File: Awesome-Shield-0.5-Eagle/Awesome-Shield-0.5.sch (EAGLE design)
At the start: 24 parts, among them J1 ARDUINO_R3_SHIELDUNO_R3_SHIEL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, SW1 SPST_TACT-EVQQ2

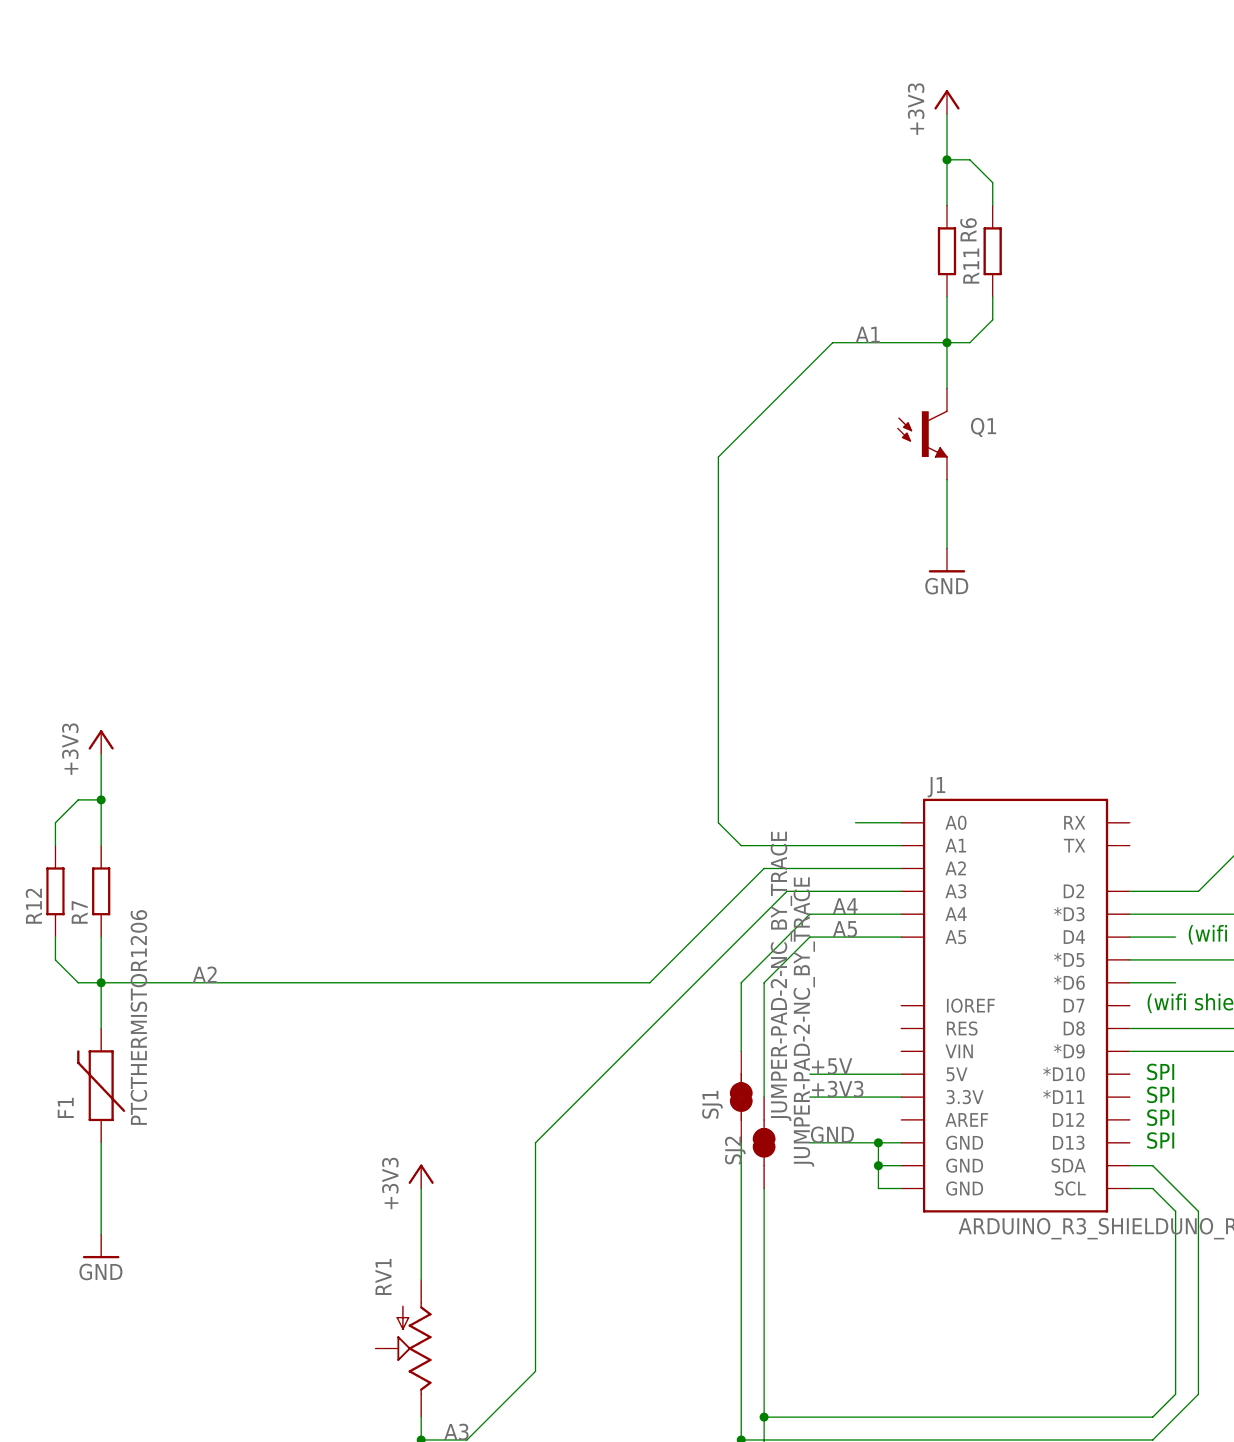
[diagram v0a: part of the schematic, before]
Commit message: changed thermistor, photodiode, and potentiometer to be powered off IOREF
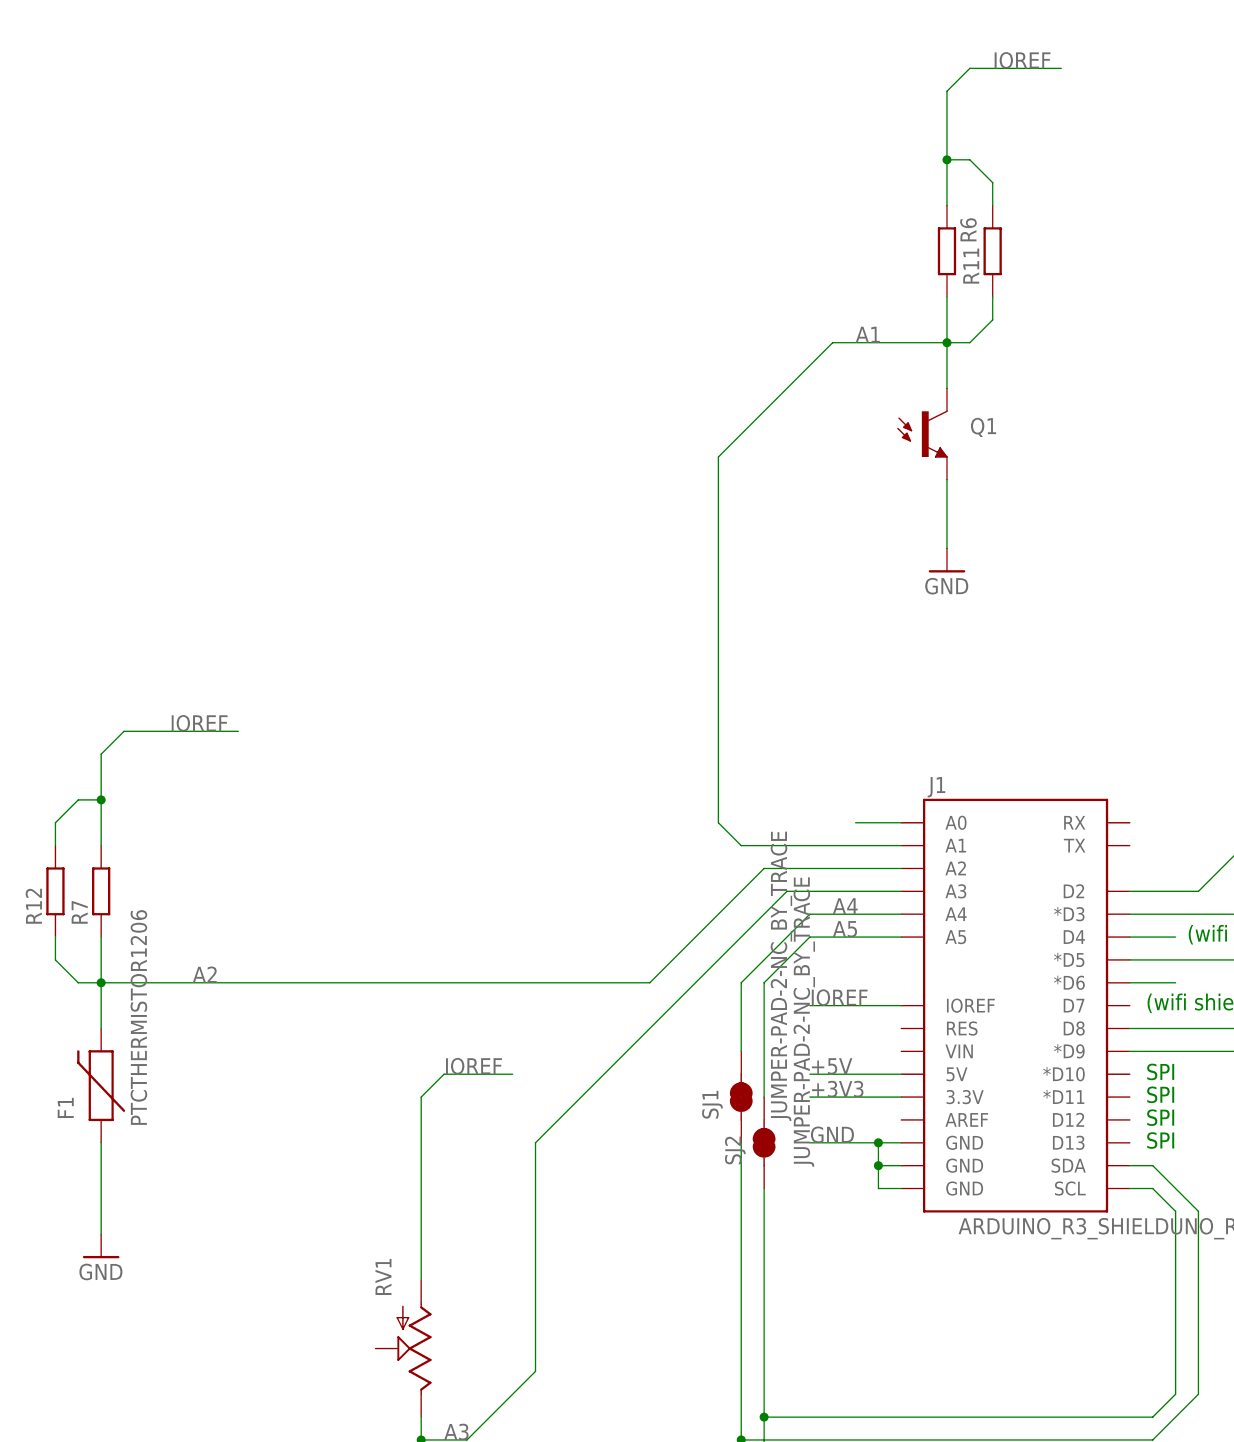
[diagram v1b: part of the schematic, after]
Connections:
- new net IOREF: J1.IOREF, R11.2, R12.2, R6.1, R7.2, RV1.A
- net +3V3: no longer R11.2, R12.2, R6.1, R7.2, RV1.A
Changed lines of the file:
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@@
 <part name="GND3" library="supply1" deviceset="GND" device=""/>
 <part name="GND4" library="supply1" deviceset="GND" device=""/>
-<part name="+3V1" library="supply1" deviceset="+3V3" device=""/>
-<part name="+3V2" library="supply1" deviceset="+3V3" device=""/>
-<part name="+3V3" library="supply1" deviceset="+3V3" device=""/>
 <part name="GND5" library="supply1" deviceset="GND" device=""/>
 <part name="GND6" library="supply1" deviceset="GND" device=""/>
@@
 <instance part="GND3" gate="1" x="93.98" y="101.6"/>
 <instance part="GND4" gate="1" x="129.54" y="68.58"/>
-<instance part="+3V1" gate="G$1" x="93.98" y="160.02"/>
-<instance part="+3V2" gate="G$1" x="129.54" y="111.76"/>
-<instance part="+3V3" gate="G$1" x="187.96" y="231.14"/>
 <instance part="GND5" gate="1" x="269.24" y="190.5"/>
 <instance part="GND6" gate="1" x="165.1" y="45.72"/>
@@
 <net name="+3V3" class="0">
 <segment>
-<pinref part="+3V3" gate="G$1" pin="+3V3"/>
-<pinref part="R6" gate="G$1" pin="1"/>
-<wire x1="187.96" y1="228.6" x2="187.96" y2="223.52" width="0.1524" layer="91"/>
-<pinref part="R11" gate="G$1" pin="2"/>
-<wire x1="187.96" y1="223.52" x2="187.96" y2="218.44" width="0.1524" layer="91"/>
-<wire x1="193.04" y1="218.44" x2="193.04" y2="220.98" width="0.1524" layer="91"/>
-<wire x1="193.04" y1="220.98" x2="190.5" y2="223.52" width="0.1524" layer="91"/>
-<wire x1="190.5" y1="223.52" x2="187.96" y2="223.52" width="0.1524" layer="91"/>
-<junction x="187.96" y="223.52"/>
-</segment>
-<segment>
-<pinref part="+3V1" gate="G$1" pin="+3V3"/>
-<pinref part="R7" gate="G$1" pin="2"/>
-<wire x1="93.98" y1="157.48" x2="93.98" y2="152.4" width="0.1524" layer="91"/>
-<pinref part="R12" gate="G$1" pin="2"/>
-<wire x1="93.98" y1="152.4" x2="93.98" y2="147.32" width="0.1524" layer="91"/>
-<wire x1="88.9" y1="147.32" x2="88.9" y2="149.86" width="0.1524" layer="91"/>
-<wire x1="88.9" y1="149.86" x2="91.44" y2="152.4" width="0.1524" layer="91"/>
-<wire x1="91.44" y1="152.4" x2="93.98" y2="152.4" width="0.1524" layer="91"/>
-<junction x="93.98" y="152.4"/>
-</segment>
-<segment>
-<pinref part="+3V2" gate="G$1" pin="+3V3"/>
-<wire x1="129.54" y1="109.22" x2="129.54" y2="99.06" width="0.1524" layer="91"/>
-<pinref part="RV1" gate="G$1" pin="A"/>
-</segment>
-<segment>
 <pinref part="J1" gate="G$1" pin="3.3V"/>
 <wire x1="182.88" y1="119.38" x2="172.72" y2="119.38" width="0.1524" layer="91"/>
@@
 </segment>
 </net>
+<net name="IOREF" class="0">
+<segment>
+<pinref part="R7" gate="G$1" pin="2"/>
+<wire x1="93.98" y1="157.48" x2="93.98" y2="152.4" width="0.1524" layer="91"/>
+<pinref part="R12" gate="G$1" pin="2"/>
+<wire x1="93.98" y1="152.4" x2="93.98" y2="147.32" width="0.1524" layer="91"/>
+<wire x1="88.9" y1="147.32" x2="88.9" y2="149.86" width="0.1524" layer="91"/>
+<wire x1="88.9" y1="149.86" x2="91.44" y2="152.4" width="0.1524" layer="91"/>
+<wire x1="91.44" y1="152.4" x2="93.98" y2="152.4" width="0.1524" layer="91"/>
+<junction x="93.98" y="152.4"/>
+<wire x1="93.98" y1="157.48" x2="96.52" y2="160.02" width="0.1524" layer="91"/>
+<wire x1="96.52" y1="160.02" x2="109.22" y2="160.02" width="0.1524" layer="91"/>
+<label x="101.6" y="160.02" size="1.778" layer="95"/>
+</segment>
+<segment>
+<pinref part="J1" gate="G$1" pin="IOREF"/>
+<wire x1="182.88" y1="129.54" x2="172.72" y2="129.54" width="0.1524" layer="91"/>
+<label x="172.72" y="129.54" size="1.778" layer="95"/>
+</segment>
+<segment>
+<pinref part="RV1" gate="G$1" pin="A"/>
+<wire x1="129.54" y1="99.06" x2="129.54" y2="119.38" width="0.1524" layer="91"/>
+<wire x1="129.54" y1="119.38" x2="132.08" y2="121.92" width="0.1524" layer="91"/>
+<wire x1="132.08" y1="121.92" x2="139.7" y2="121.92" width="0.1524" layer="91"/>
+<label x="132.08" y="121.92" size="1.778" layer="95"/>
+</segment>
+<segment>
+<pinref part="R6" gate="G$1" pin="1"/>
+<wire x1="187.96" y1="231.14" x2="187.96" y2="223.52" width="0.1524" layer="91"/>
+<pinref part="R11" gate="G$1" pin="2"/>
+<wire x1="187.96" y1="223.52" x2="187.96" y2="218.44" width="0.1524" layer="91"/>
+<wire x1="193.04" y1="218.44" x2="193.04" y2="220.98" width="0.1524" layer="91"/>
+<wire x1="193.04" y1="220.98" x2="190.5" y2="223.52" width="0.1524" layer="91"/>
+<wire x1="190.5" y1="223.52" x2="187.96" y2="223.52" width="0.1524" layer="91"/>
+<junction x="187.96" y="223.52"/>
+<wire x1="187.96" y1="231.14" x2="190.5" y2="233.68" width="0.1524" layer="91"/>
+<wire x1="190.5" y1="233.68" x2="200.66" y2="233.68" width="0.1524" layer="91"/>
+<label x="193.04" y="233.68" size="1.778" layer="95"/>
+</segment>
+</net>

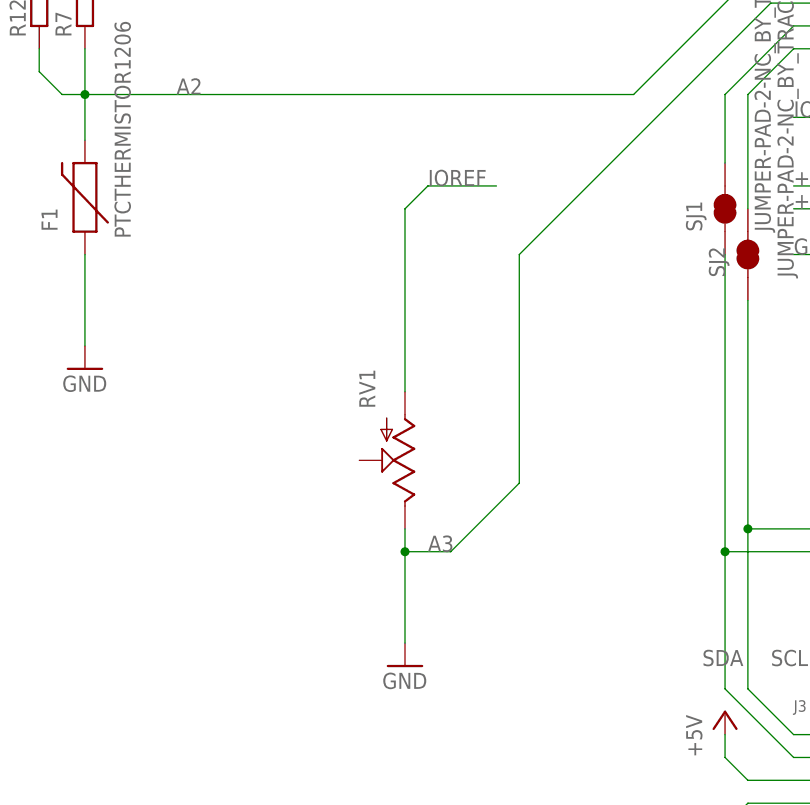
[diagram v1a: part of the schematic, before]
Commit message: corrected pot circuit in schematic
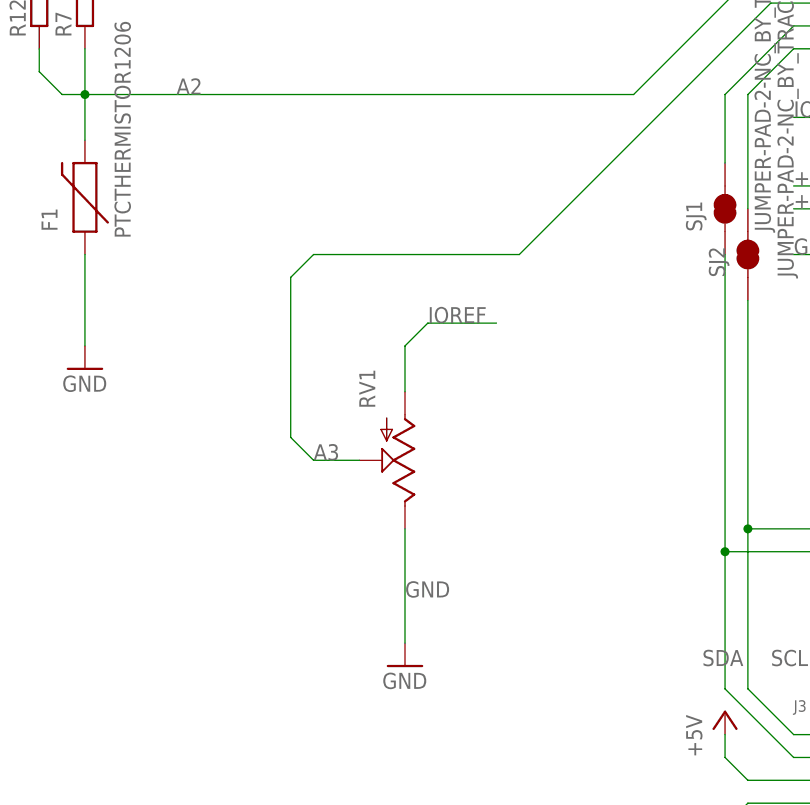
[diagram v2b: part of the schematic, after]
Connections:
- net A3: now also RV1.S; no longer RV1.E
- net GND: now also RV1.E
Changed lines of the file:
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@@
 <label x="172.72" y="114.3" size="1.778" layer="95"/>
+</segment>
+<segment>
+<pinref part="GND4" gate="1" pin="GND"/>
+<pinref part="RV1" gate="G$1" pin="E"/>
+<wire x1="129.54" y1="83.82" x2="129.54" y2="71.12" width="0.1524" layer="91"/>
+<label x="129.54" y="76.2" size="1.778" layer="95"/>
 </segment>
 </net>
@@
 <net name="A3" class="0">
 <segment>
-<pinref part="GND4" gate="1" pin="GND"/>
-<wire x1="129.54" y1="83.82" x2="129.54" y2="81.28" width="0.1524" layer="91"/>
-<wire x1="129.54" y1="81.28" x2="129.54" y2="71.12" width="0.1524" layer="91"/>
-<junction x="129.54" y="81.28"/>
-<wire x1="129.54" y1="81.28" x2="134.62" y2="81.28" width="0.1524" layer="91"/>
-<wire x1="134.62" y1="81.28" x2="142.24" y2="88.9" width="0.1524" layer="91"/>
-<wire x1="142.24" y1="88.9" x2="142.24" y2="114.3" width="0.1524" layer="91"/>
 <wire x1="142.24" y1="114.3" x2="170.18" y2="142.24" width="0.1524" layer="91"/>
 <pinref part="J1" gate="G$1" pin="A3"/>
 <wire x1="170.18" y1="142.24" x2="182.88" y2="142.24" width="0.1524" layer="91"/>
-<pinref part="RV1" gate="G$1" pin="E"/>
-<label x="132.08" y="81.28" size="1.778" layer="95"/>
+<wire x1="142.24" y1="114.3" x2="119.38" y2="114.3" width="0.1524" layer="91"/>
+<wire x1="119.38" y1="114.3" x2="116.84" y2="111.76" width="0.1524" layer="91"/>
+<wire x1="116.84" y1="111.76" x2="116.84" y2="93.98" width="0.1524" layer="91"/>
+<wire x1="116.84" y1="93.98" x2="119.38" y2="91.44" width="0.1524" layer="91"/>
+<pinref part="RV1" gate="G$1" pin="S"/>
+<wire x1="119.38" y1="91.44" x2="124.46" y2="91.44" width="0.1524" layer="91"/>
+<label x="119.38" y="91.44" size="1.778" layer="95"/>
 </segment>
 </net>
@@
 <segment>
 <pinref part="RV1" gate="G$1" pin="A"/>
-<wire x1="129.54" y1="99.06" x2="129.54" y2="119.38" width="0.1524" layer="91"/>
-<wire x1="129.54" y1="119.38" x2="132.08" y2="121.92" width="0.1524" layer="91"/>
-<wire x1="132.08" y1="121.92" x2="139.7" y2="121.92" width="0.1524" layer="91"/>
-<label x="132.08" y="121.92" size="1.778" layer="95"/>
-</segment>
-<segment>
+<wire x1="129.54" y1="99.06" x2="129.54" y2="104.14" width="0.1524" layer="91"/>
+<wire x1="129.54" y1="104.14" x2="132.08" y2="106.68" width="0.1524" layer="91"/>
+<wire x1="132.08" y1="106.68" x2="139.7" y2="106.68" width="0.1524" layer="91"/>
+<label x="132.08" y="106.68" size="1.778" layer="95"/>
+</segment>
+<segment>
